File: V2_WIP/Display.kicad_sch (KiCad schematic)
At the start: 16 parts, among them U2 TPS613222ADBVR, U4 HT16k33, U5 7seg_1x1_rgb, U6 7seg_1x1_rgb, U7 7seg_1x1_rgb, U8 KW4-804AGB

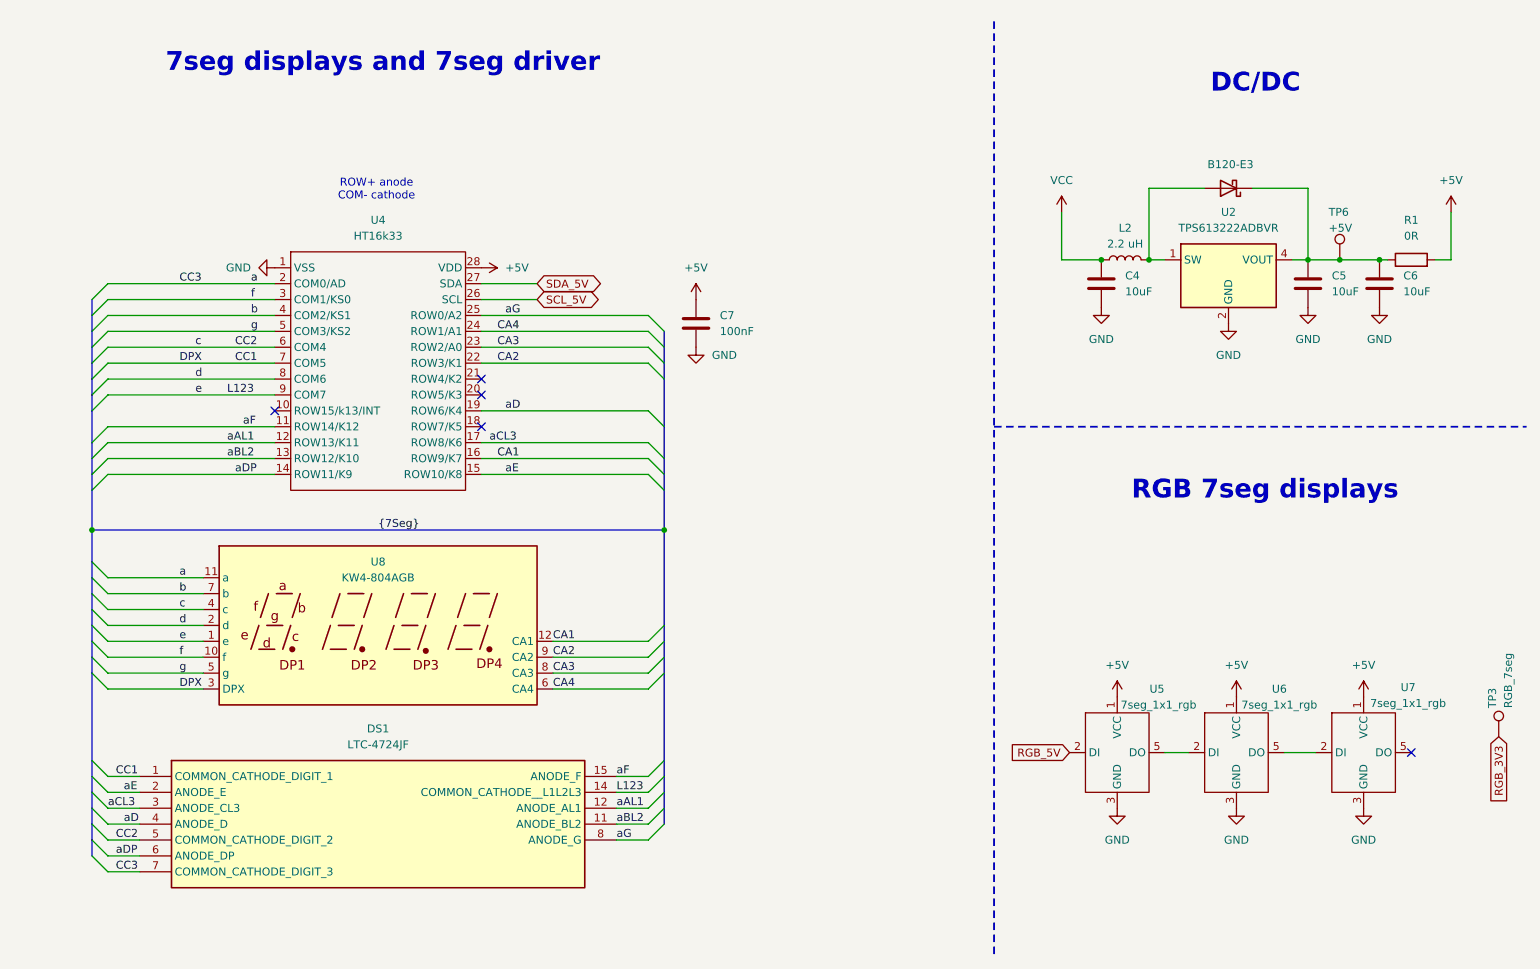
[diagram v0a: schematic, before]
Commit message: Cleaned schematic
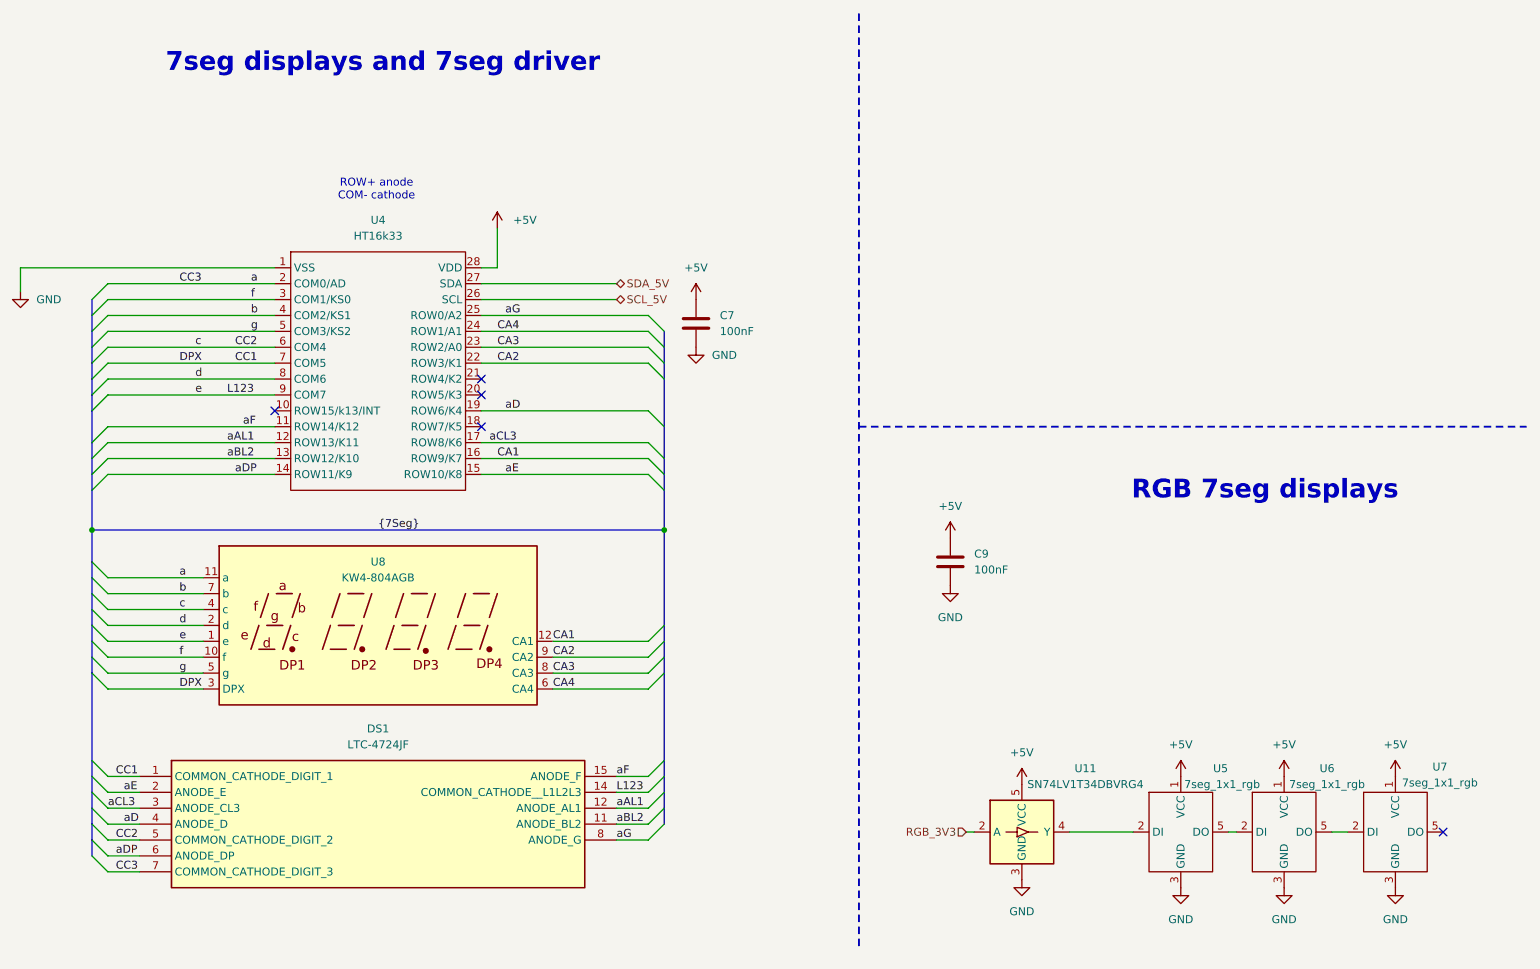
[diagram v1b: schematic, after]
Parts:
- removed C4, C5, C6: 10uF, Capacitor_SMD:C_0603_1608Metric_Pad1.08x0.95mm_HandSolder, symbol Device:C
- removed D2: B120-E3, Diode_SMD:D_SMA, symbol Diode:B120-E3
- removed L2: 2.2 uH, Inductor_SMD:L_1008_2520Metric_Pad1.43x2.20mm_HandSolder, symbol Device:L
- removed R1: 0R, Resistor_SMD:R_0805_2012Metric_Pad1.20x1.40mm_HandSolder, symbol Device:R
- removed TP3: RGB_7seg, TestPoint:TestPoint_Pad_D1.5mm, symbol Connector:TestPoint
- removed TP6: +5V, TestPoint:TestPoint_Pad_D1.5mm, symbol Connector:TestPoint
- removed U2: TPS613222ADBVR, Package_TO_SOT_SMD:SOT-23-5, symbol Regulator_Switching:TPS613226ADBV
- added C9: 100nF, Capacitor_SMD:C_0805_2012Metric_Pad1.18x1.45mm_HandSolder, symbol Device:C
- added U11: SN74LV1T34DBVRG4, Package_TO_SOT_SMD:SOT-23-5, symbol Logic_LevelTranslator:SN74LV1T34DBV
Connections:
- net +5V: now also C9.2, U11.5 (VCC)
- net GND: now also C9.1, U11.3 (GND)
- net RGB_3V3: now also U11.2 (A)
- net RGB_5V: no longer names the net of U5.2 (DI)
- net RGB_5V: now also U11.4 (Y)
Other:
- note removed: "DC/DC"
- moved on the sheet: U5, U6, U7

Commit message: minor schematic changes
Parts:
- added TP403: RGB_5V, TestPoint:TestPoint_Pad_D1.5mm, symbol Connector:TestPoint
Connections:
- net at U11.4 (Y), U5.2 (DI): now also TP403.1
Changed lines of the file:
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@@
+		(color 0 0 0 0)
+	)
+	(junction
+		(at 215.9 144.78)
+		(diameter 0)
 		(color 0 0 0 0)
 	)
@@
 	(wire
 		(pts
-			(xy 210.82 144.78) (xy 220.98 144.78)
+			(xy 210.82 144.78) (xy 215.9 144.78)
 		)
 		(stroke
@@
 		(pts
 			(xy 146.05 140.97) (xy 146.05 143.51)
+		)
+		(stroke
+			(width 0)
+			(type default)
+		)
+	)
+	(wire
+		(pts
+			(xy 215.9 144.78) (xy 220.98 144.78)
 		)
 		(stroke
@@
 					(unit 1)
 				)
+			)
+		)
+	)
+	(symbol
+		(lib_id "Connector:TestPoint")
+		(at 215.9 144.78 180)
+		(unit 1)
+		(exclude_from_sim no)
+		(in_bom yes)
+		(on_board yes)
+		(dnp no)
+		(property "Reference" "TP403"
+			(at 216.916 149.352 90)
+			(effects
+				(font
+					(size 1.27 1.27)
+				)
+				(justify left)
+			)
+		)
+		(property "Value" "RGB_5V"
+			(at 214.376 149.352 90)
+			(effects
+				(font
+					(size 1.27 1.27)
+				)
+				(justify left)
+			)
+		)
+		(property "Footprint" "TestPoint:TestPoint_Pad_D1.5mm"
+			(at 210.82 144.78 0)
+			(effects
+				(font
+					(size 1.27 1.27)
+				)
+				(hide yes)
+			)
+		)
+		(property "Datasheet" "~"
+			(at 210.82 144.78 0)
+			(effects
+				(font
+					(size 1.27 1.27)
+				)
+				(hide yes)
+			)
+		)
+		(property "Description" "test point"
+			(at 215.9 144.78 0)
+			(effects
+				(font
+					(size 1.27 1.27)
+				)
+				(hide yes)
+			)
+		)
+		(pin "1"
+		)
+		(instances
+			(project "gps"
+				(path "/00526ddc-5304-4072-af1e-192a9e7e83da/944a09ba-484a-42c8-9e47-79436575a39f"
+					(reference "TP403")
+					(unit 1)
+				)

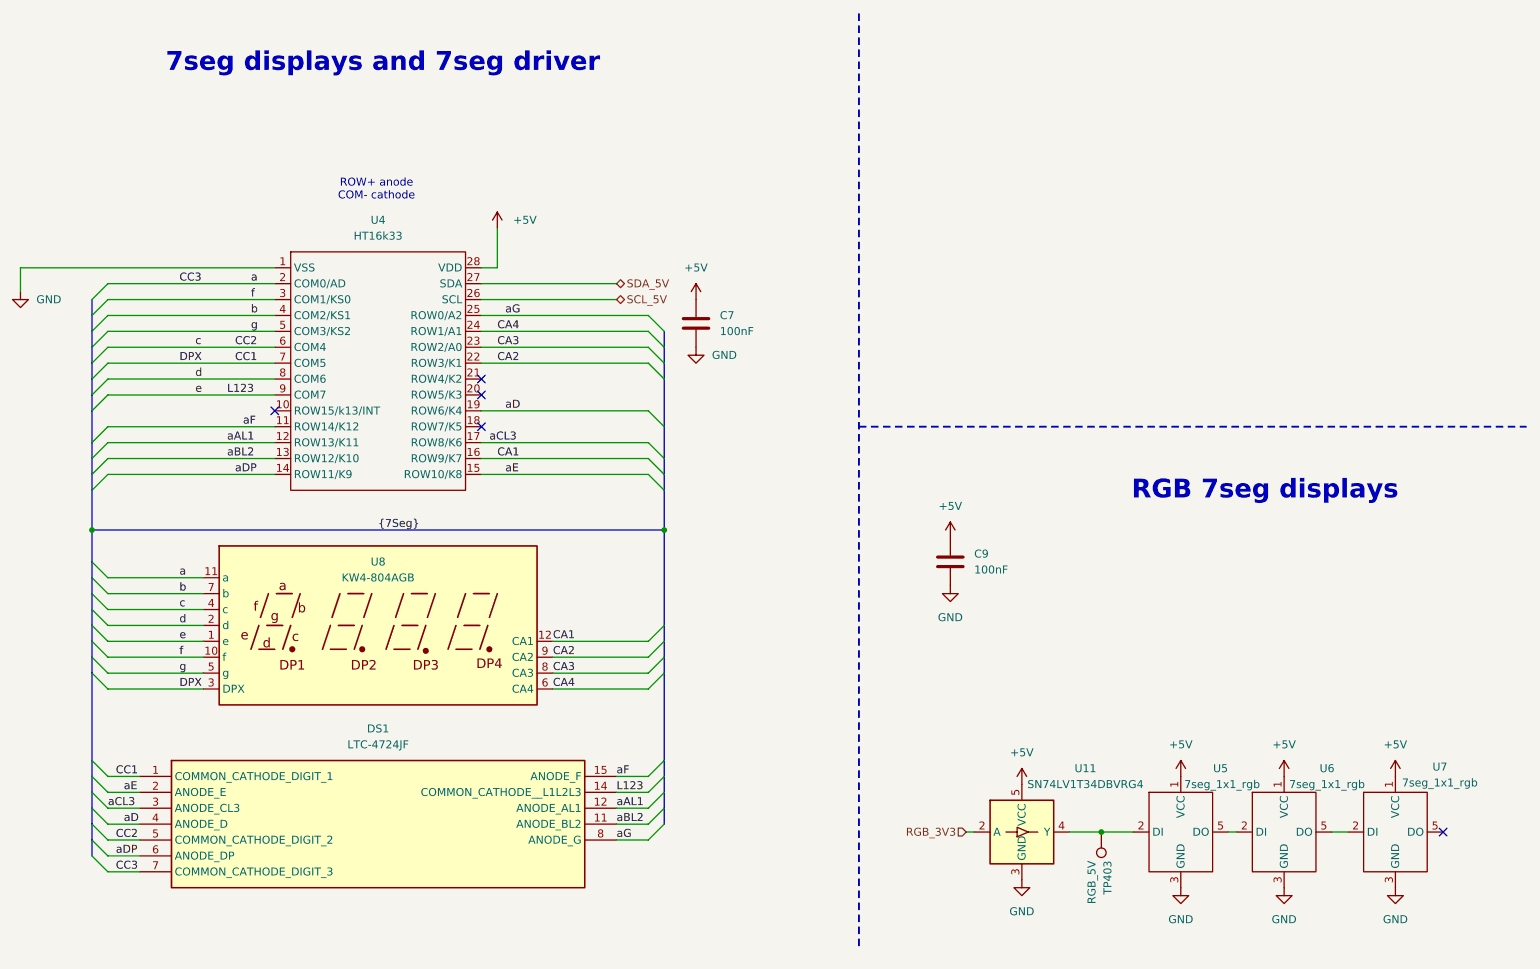
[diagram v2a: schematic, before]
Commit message: added LED indicators, light sensor, changed to CC 7seg displays
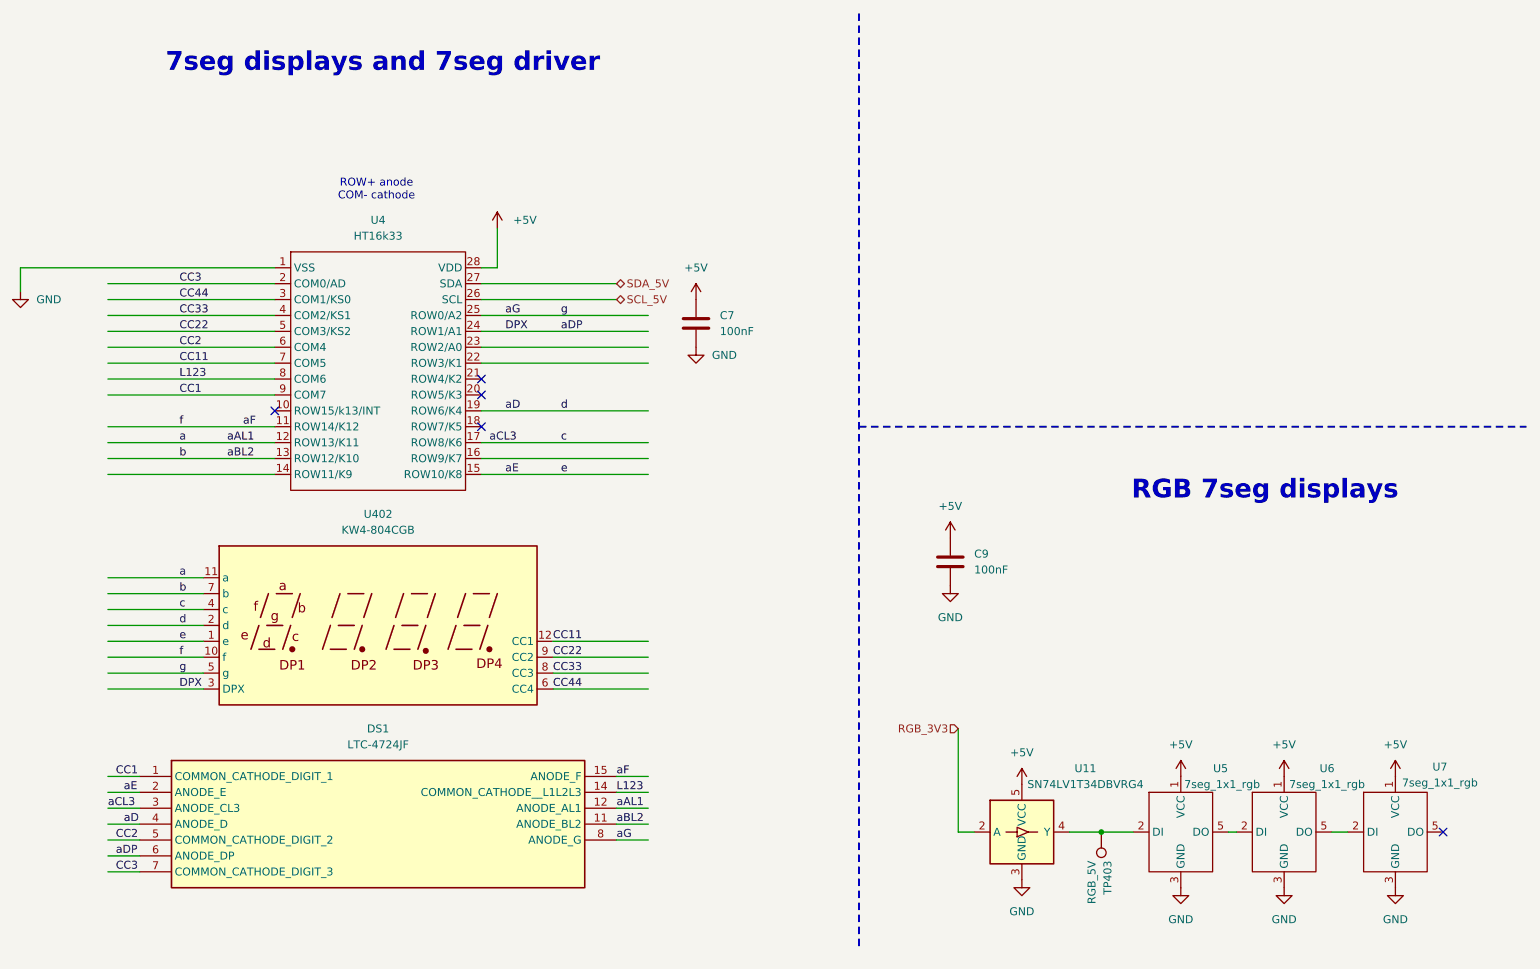
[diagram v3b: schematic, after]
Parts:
- removed U8: KW4-804AGB, 7seg_rgb:7seg_4x1, symbol Display_Character:CA56-12CGKWA
- added U402: KW4-804CGB, 7seg_rgb:7seg_4x1, symbol Display_Character:CC56-12SEKWA
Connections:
- net d is gone; now on net L123: U4.8 (COM6)
- net CC1: now also U4.9 (COM7); no longer U4.7 (COM5)
- net L123: no longer U4.9 (COM7)
- net aBL2: now also U402.7 (b)
- net aCL3: now also U402.4 (c)
- net aD: now also U402.2 (d)
- net aE: now also U402.1 (e)
- net aF: now also U402.10 (f)
- net aG: now also U402.5 (g)
- net CA1: no longer names the net of U4.16 (ROW9/K7)
- net CA2: no longer names the net of U4.22 (ROW3/K1)
- net CA3: no longer names the net of U4.23 (ROW2/A0)
- net CA4 renamed DPX
- net DPX: now also DS1.6 (ANODE_DP), U402.3 (DPX)
- net aAL1 renamed a
- net a: now also U402.11 (a)
- net aDP: no longer names the net of U4.14 (ROW11/K9)
- net aDP: no longer DS1.6 (ANODE_DP)
- net b renamed CC33
- net CC33: now also U402.8 (CC3)
- net f renamed CC44
- net CC44: now also U402.6 (CC4)
- net g renamed CC22
- net CC22: now also U402.9 (CC2)
- new net CC11: U4.7 (COM5), U402.12 (CC1)

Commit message: added USB, button
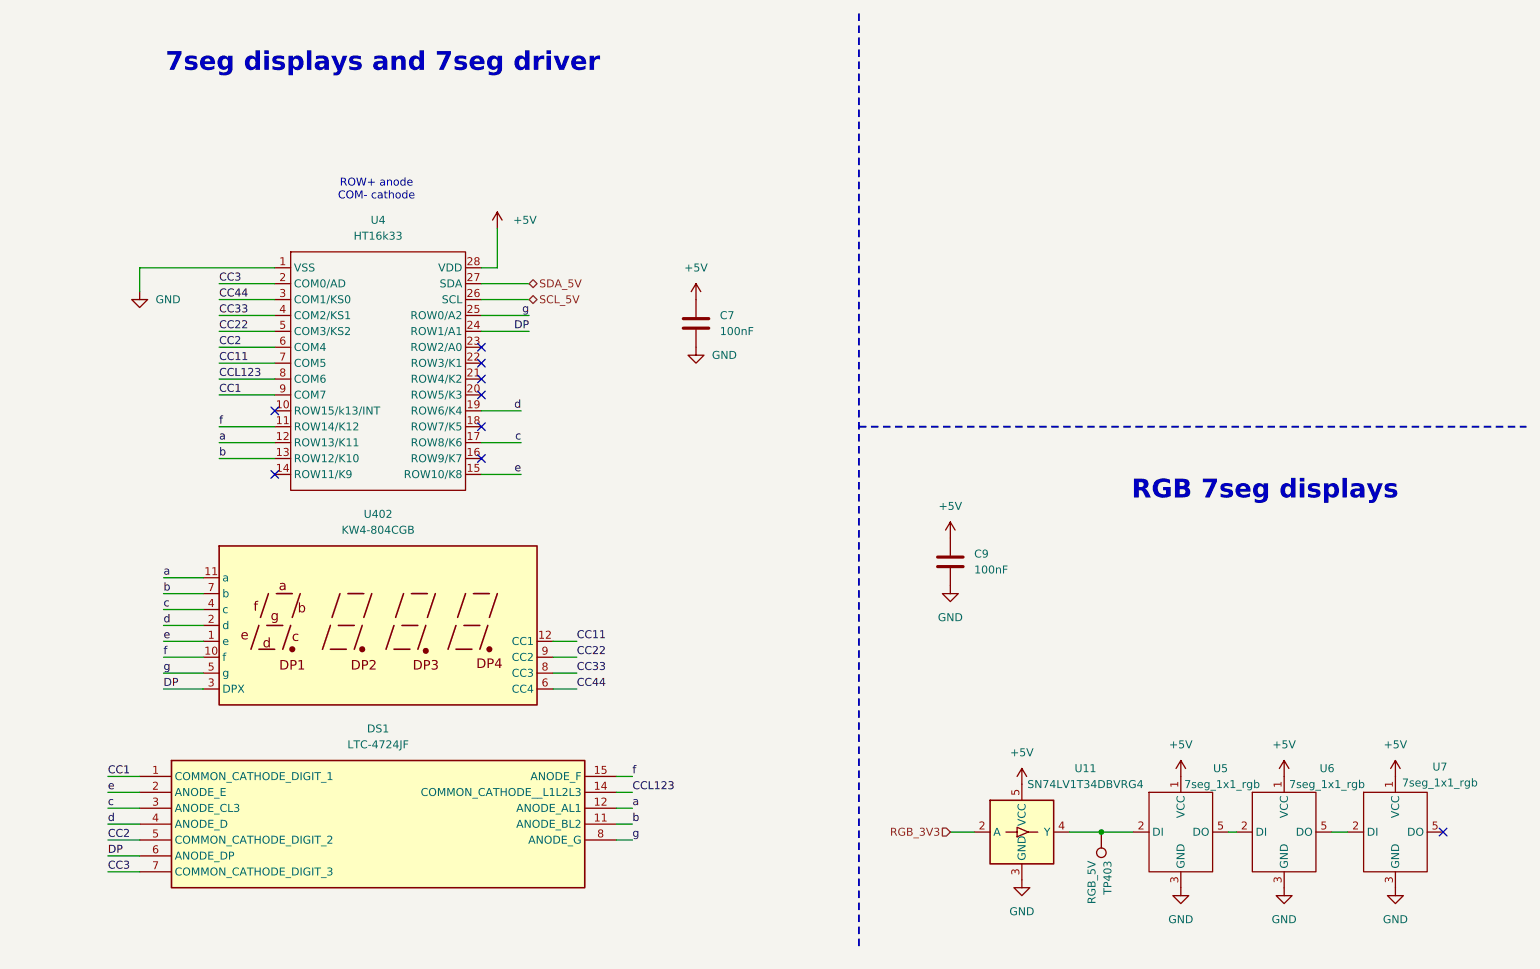
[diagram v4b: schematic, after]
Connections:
- net DPX renamed DP
- net L123 renamed CCL123
- net aBL2 renamed b
- net aCL3 renamed c
- net aD renamed d
- net aE renamed e
- net aF renamed f
- net aG renamed g
- no-connect marks 5 -> 9

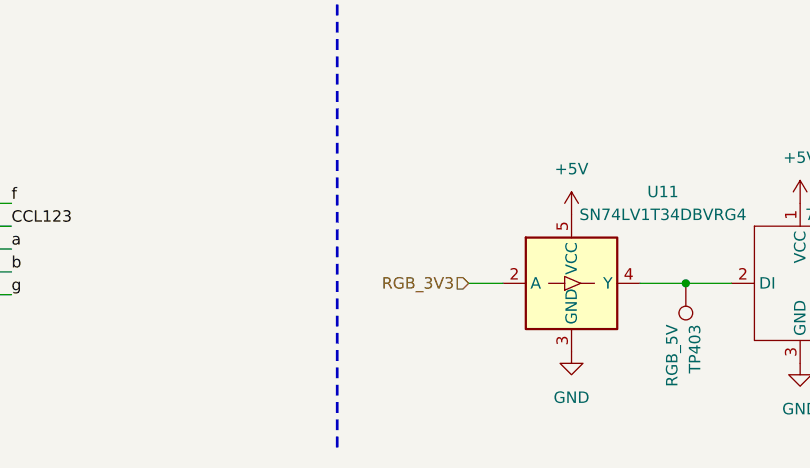
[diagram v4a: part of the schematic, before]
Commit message: Removed EEPROM, Adjusted Flash connection, renamed ESP pins and several other signals
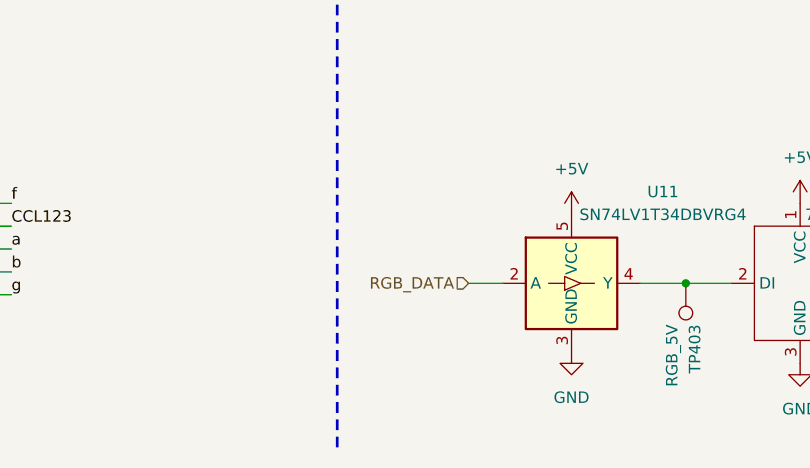
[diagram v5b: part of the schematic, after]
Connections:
- net RGB_3V3 renamed RGB_DATA
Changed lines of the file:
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@@
 		)
 	)
-	(hierarchical_label "RGB_3V3"
+	(hierarchical_label "RGB_DATA"
 		(shape input)
 		(at 191.77 144.78 180)

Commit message: finallizes schematic; pcb progress
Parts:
- added C404, C405, C406: 100nF, Capacitor_SMD:C_0805_2012Metric_Pad1.18x1.45mm_HandSolder, symbol Device:C
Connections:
- net +5V: now also C404.2, C405.2, C406.2
- net CC1: now also U4.6 (COM4); no longer U4.9 (COM7)
- net CC11: now also U4.2 (COM0/AD); no longer U4.7 (COM5)
- net CC2: now also U4.7 (COM5); no longer U4.6 (COM4)
- net CC22: now also U4.3 (COM1/KS0); no longer U4.5 (COM3/KS2)
- net CC3: now also U4.8 (COM6); no longer U4.2 (COM0/AD)
- net CC44: now also U4.5 (COM3/KS2); no longer U4.3 (COM1/KS0)
- net CCL123: now also U4.9 (COM7); no longer U4.8 (COM6)
- net DP: now also U4.18 (ROW7/K5); no longer U4.24 (ROW1/A1)
- net GND: now also C404.1, C405.1, C406.1
- net a: now also U4.25 (ROW0/A2); no longer U4.12 (ROW13/K11)
- net b: now also U4.24 (ROW1/A1); no longer U4.13 (ROW12/K10)
- net c: now also U4.23 (ROW2/A0); no longer U4.17 (ROW8/K6)
- net d: now also U4.22 (ROW3/K1); no longer U4.19 (ROW6/K4)
- net e: now also U4.21 (ROW4/K2); no longer U4.15 (ROW10/K8)
- net f: now also U4.20 (ROW5/K3); no longer U4.11 (ROW14/K12)
- net g: now also U4.19 (ROW6/K4); no longer U4.25 (ROW0/A2)
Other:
- moved on the sheet: C9
